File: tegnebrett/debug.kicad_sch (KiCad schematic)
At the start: 21 parts, among them U1 XC7A100T-2FTG256I, U2 Oscillator 100MHz

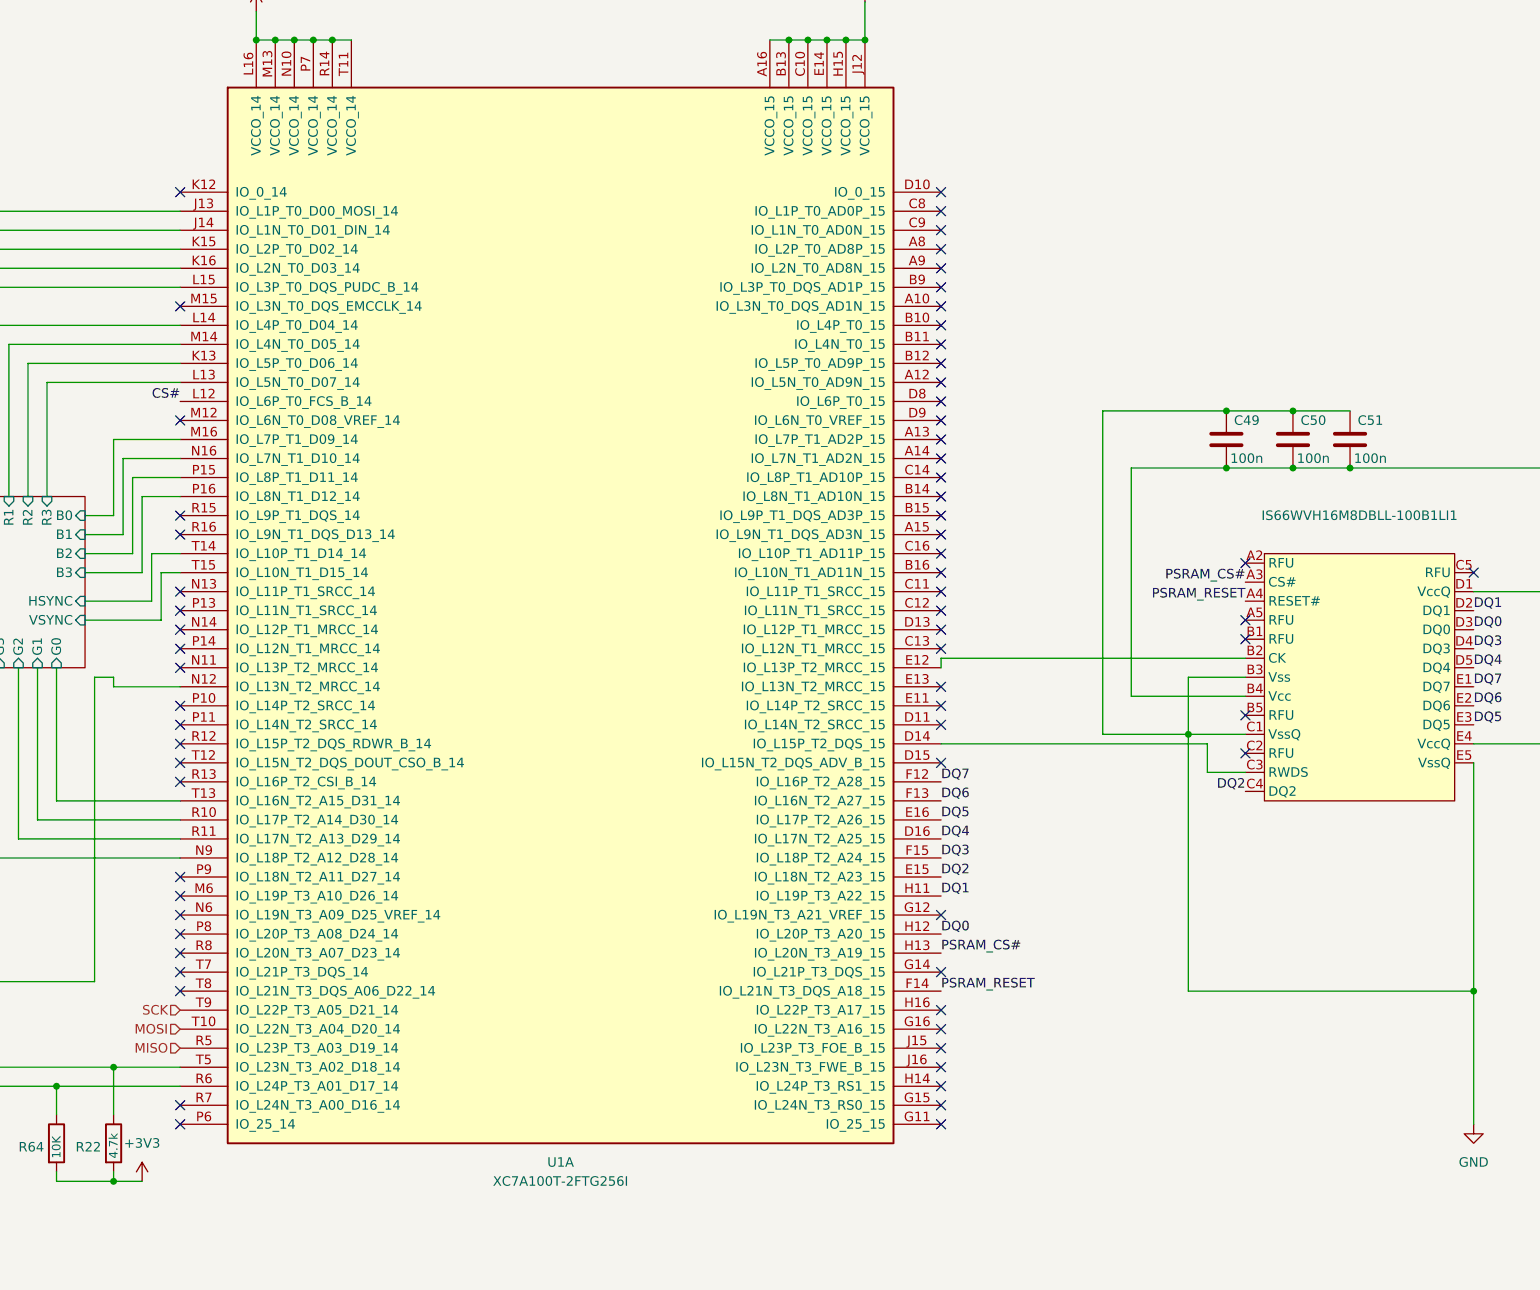
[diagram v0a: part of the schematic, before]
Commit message: feat: PCB update
Main additions:

- Added LEDs to Power Supply, MCU and FPGA.
The resistor values will depend on the specific LEDs we buy.
Red LEDs need a different resistor value than blue LEDs, etc.

- Added a bunch of buttons to the MCU
It doesn't hurt to have some redundancy here.

- Added header pins
Allows us to easily reach GPIO pins on the MCU and the FPGA.
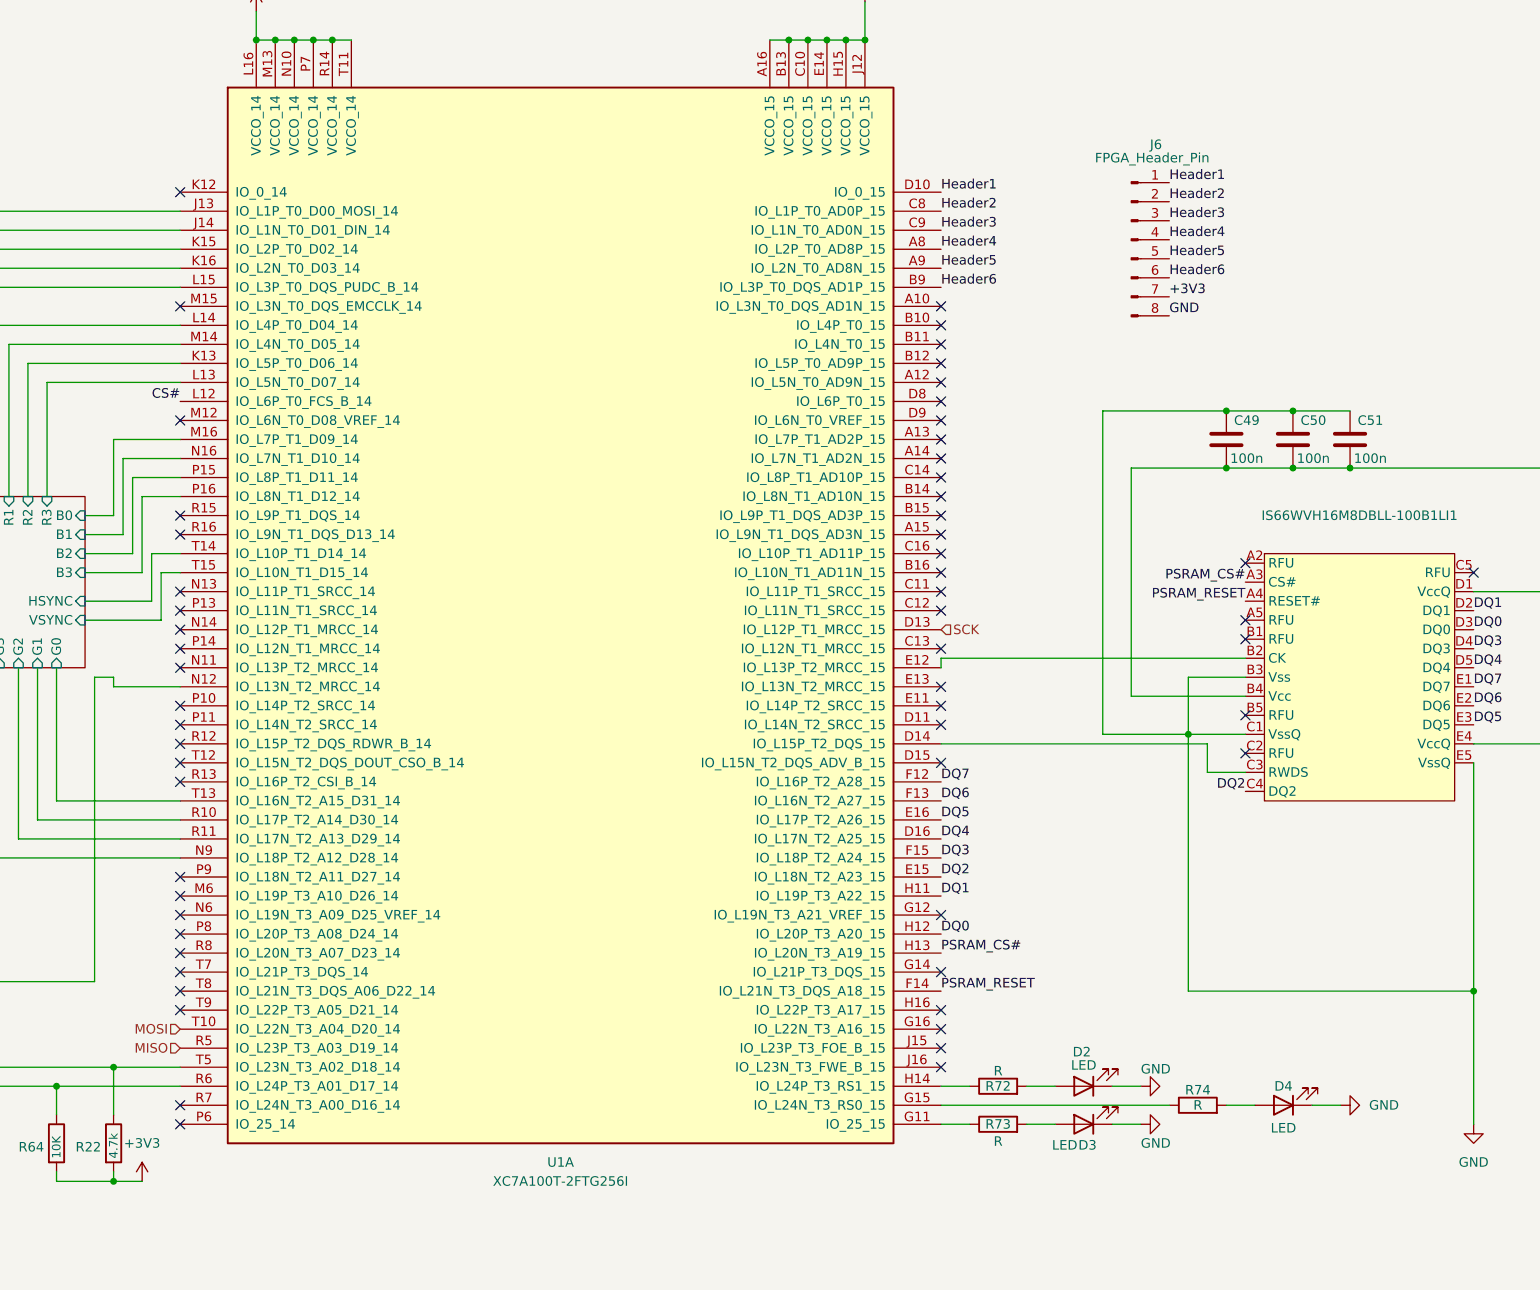
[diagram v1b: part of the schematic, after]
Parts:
- added D2, D3, D4: LED, symbol Device:LED
- added J6: FPGA_Header_Pin, symbol Connector:Conn_01x08_Pin
- added R72, R73, R74: R, symbol Device:R
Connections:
- net +3V3: now also J6.7 (Pin_7)
- net GND: now also D2.1 (K), D3.1 (K), D4.1 (K), J6.8 (Pin_8)
- net SCK: now also U1.D13 (IO_L12P_T1_MRCC_15); no longer U1.T9 (IO_L22P_T3_A05_D21_14)
- net Header4: now reaches U1.A8 (IO_L2P_T0_AD8P_15)
- net Header4: now also J6.4 (Pin_4)
- net Header5: now reaches U1.A9 (IO_L2N_T0_AD8N_15)
- net Header5: now also J6.5 (Pin_5)
- net Header6: now reaches U1.B9 (IO_L3P_T0_DQS_AD1P_15)
- net Header6: now also J6.6 (Pin_6)
- net Header2: now reaches U1.C8 (IO_L1P_T0_AD0P_15)
- net Header2: now also J6.2 (Pin_2)
- net Header3: now reaches U1.C9 (IO_L1N_T0_AD0N_15)
- net Header3: now also J6.3 (Pin_3)
- net Header1: now reaches U1.D10 (IO_0_15)
- net Header1: now also J6.1 (Pin_1)
- net at U1.G11 (IO_25_15): now also R73.1
- net at U1.G15 (IO_L24N_T3_RS0_15): now also R74.1
- net at U1.H14 (IO_L24P_T3_RS1_15): now also R72.1
- new net: D4.2 (A), R74.2
- new net: D3.2 (A), R73.2
- new net: D2.2 (A), R72.2
- no-connect marks 142 -> 133

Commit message: feat: add some footprints
Added footprints to vertical 8pin connectors and so forth.
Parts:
- J6: footprint (none) -> Connector_PinHeader_2.54mm:PinHeader_1x08_P2.54mm_Vertical
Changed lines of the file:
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@@
 			)
 		)
-		(property "Footprint" ""
+		(property "Footprint" "Connector_PinHeader_2.54mm:PinHeader_1x08_P2.54mm_Vertical"
 			(at 345.44 54.61 0)
 			(effects

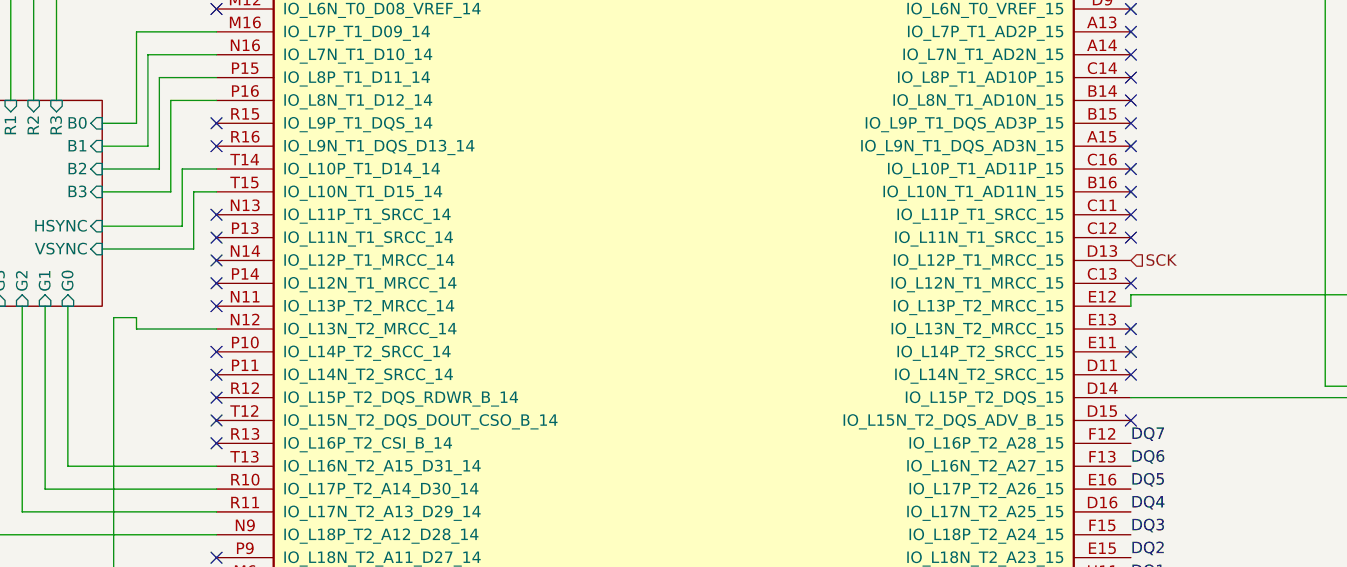
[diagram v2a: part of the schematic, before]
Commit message: feat: add 3d-models to custom footprints
6pin and 45pin, USB-A.
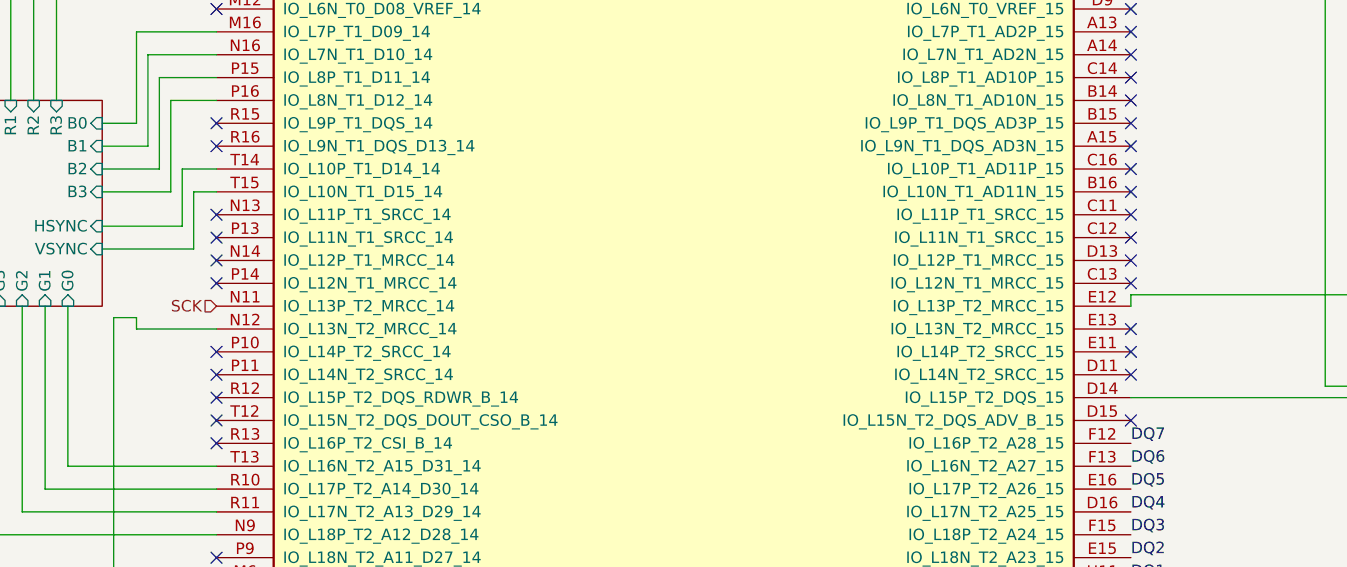
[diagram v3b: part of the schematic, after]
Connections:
- net SCK: now also U1.N11 (IO_L13P_T2_MRCC_14); no longer U1.D13 (IO_L12P_T1_MRCC_15)
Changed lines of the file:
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@@
-	)
-	(no_connect
-		(at 218.44 111.76)
 	)
 	(no_connect
@@
 	(no_connect
 		(at 16.51 152.4)
+	)
+	(no_connect
+		(at 320.04 106.68)
 	)
 	(no_connect
@@
 	(hierarchical_label "SCK"
 		(shape input)
-		(at 320.04 106.68 0)
-		(effects
-			(font
-				(size 1.27 1.27)
-			)
-			(justify left)
-		)
-	)
+		(at 218.44 111.76 180)
+		(effects
+			(font
+				(size 1.27 1.27)
+			)
+			(justify right)
+		)
+	)

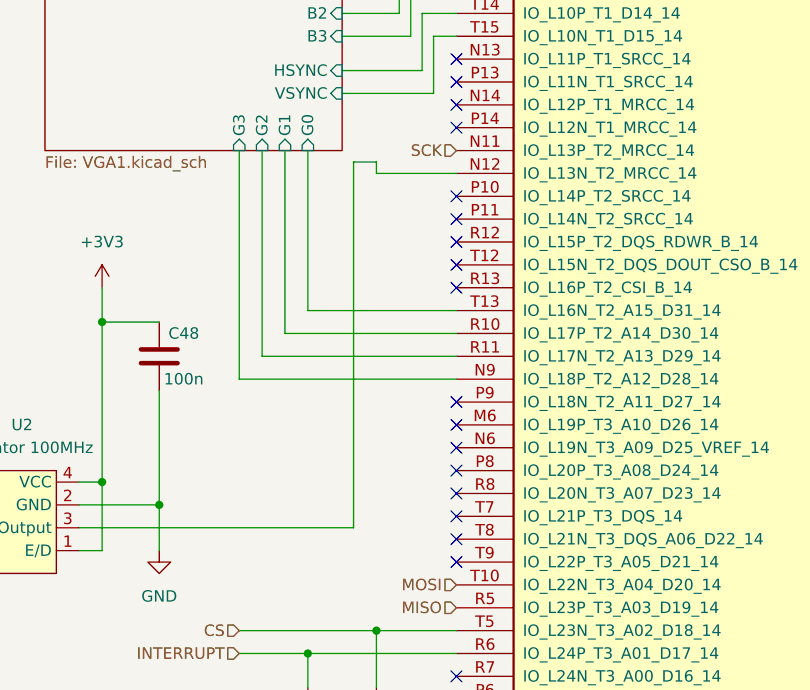
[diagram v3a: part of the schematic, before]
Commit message: feat: add 100MHz oscillator footprint
Additionally add the footprint to PCB.
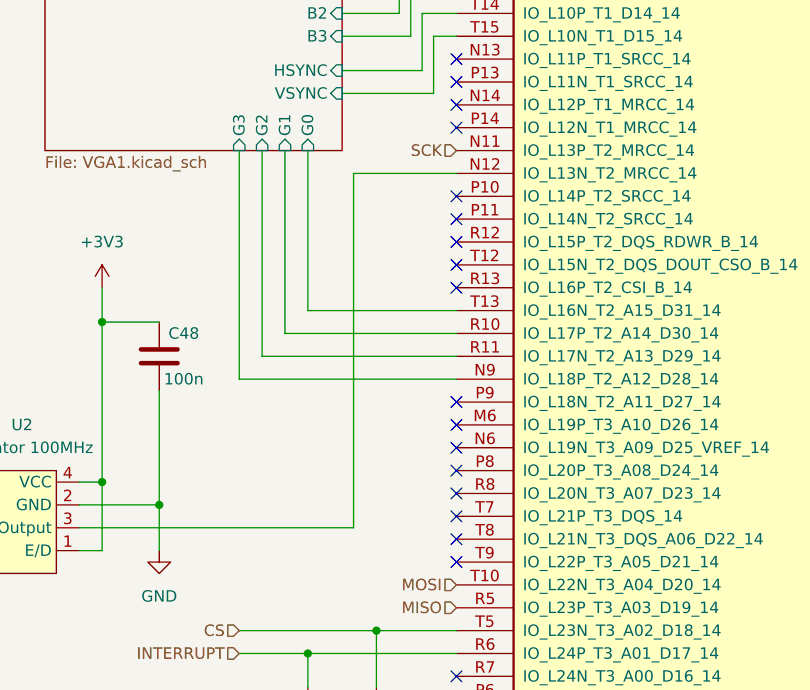
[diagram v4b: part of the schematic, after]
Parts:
- U2: footprint (none) -> tegnebrett_modules:CWX813-100.0M_CNW
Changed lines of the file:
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@@
-	(wire
-		(pts
-			(xy 209.55 113.03) (xy 209.55 114.3)
-		)
-		(stroke
-			(width 0)
-			(type default)
-		)
-	)
 	(wire
 		(pts
@@
 	(wire
 		(pts
-			(xy 207.01 113.03) (xy 209.55 113.03)
+			(xy 207.01 114.3) (xy 218.44 114.3)
 		)
 		(stroke
@@
 	(wire
 		(pts
-			(xy 207.01 153.67) (xy 207.01 113.03)
+			(xy 207.01 153.67) (xy 207.01 114.3)
 		)
 		(stroke
@@
 		(pts
 			(xy 132.08 60.96) (xy 173.99 60.96)
-		)
-		(stroke
-			(width 0)
-			(type default)
-		)
-	)
-	(wire
-		(pts
-			(xy 209.55 114.3) (xy 218.44 114.3)
 		)
 		(stroke
@@
 			)
 		)
-		(property "Footprint" ""
+		(property "Footprint" "tegnebrett_modules:CWX813-100.0M_CNW"
 			(at 173.99 144.78 0)
 			(effects

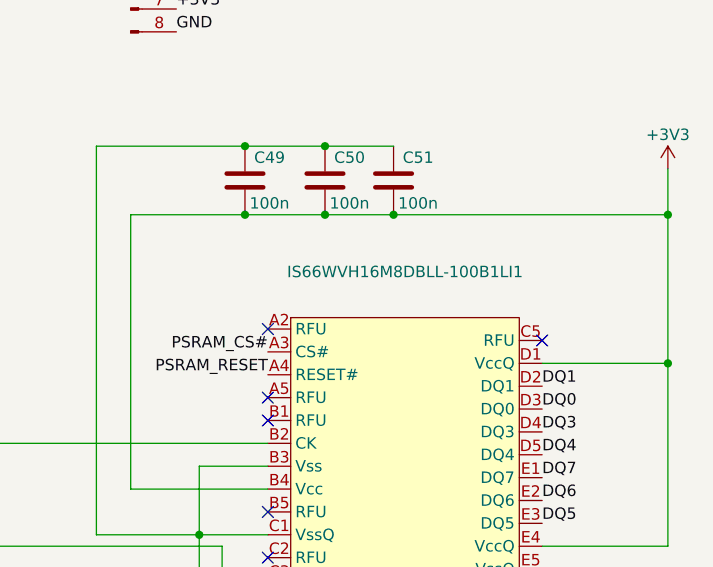
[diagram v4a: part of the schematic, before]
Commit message: feat: add psram footprint and add to PCB
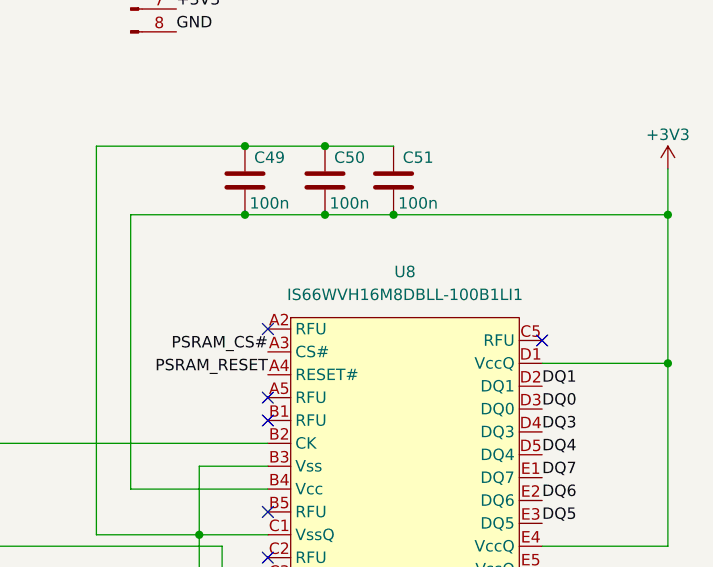
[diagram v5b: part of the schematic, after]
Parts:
- U8: renamed from IS66WVH16M8DBLL-100B1LI1; value ~ -> IS66WVH16M8DBLL-100B1LI1
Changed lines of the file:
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@@
 		(dnp no)
 		(fields_autoplaced yes)
-		(property "Reference" "IS66WVH16M8DBLL-100B1LI1"
+		(property "Reference" "U8"
 			(at 375.92 91.44 0)
 			(effects
@@
 			)
 		)
-		(property "Value" "~"
+		(property "Value" "IS66WVH16M8DBLL-100B1LI1"
 			(at 375.92 93.98 0)
 			(effects
@@
 			(project "getting-started"
 				(path "/d9a31669-c5f1-42a7-9461-3df04b9a4e62/5e0df967-c6b5-4cdf-8fe6-93251df44e99"
-					(reference "IS66WVH16M8DBLL-100B1LI1")
+					(reference "U8")
 					(unit 1)
 				)

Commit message: feat: add FPGA footprint and add footprint to PCB
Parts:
- U1: footprint (none) -> tegnebrett_modules:fpga
- U8: footprint (none) -> tegnebrett_modules:psram
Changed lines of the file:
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@@
 			)
 		)
-		(property "Footprint" ""
+		(property "Footprint" "tegnebrett_modules:fpga"
 			(at 269.24 101.6 0)
 			(effects
@@
 			)
 		)
-		(property "Footprint" ""
+		(property "Footprint" "tegnebrett_modules:fpga"
 			(at 67.31 205.74 0)
 			(effects
@@
 			)
 		)
-		(property "Footprint" ""
+		(property "Footprint" "tegnebrett_modules:psram"
 			(at 363.22 96.52 0)
 			(effects
@@
 			)
 		)
-		(property "Footprint" ""
+		(property "Footprint" "tegnebrett_modules:fpga"
 			(at 46.99 73.66 0)
 			(effects
